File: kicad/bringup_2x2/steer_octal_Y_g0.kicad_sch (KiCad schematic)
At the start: 42 parts

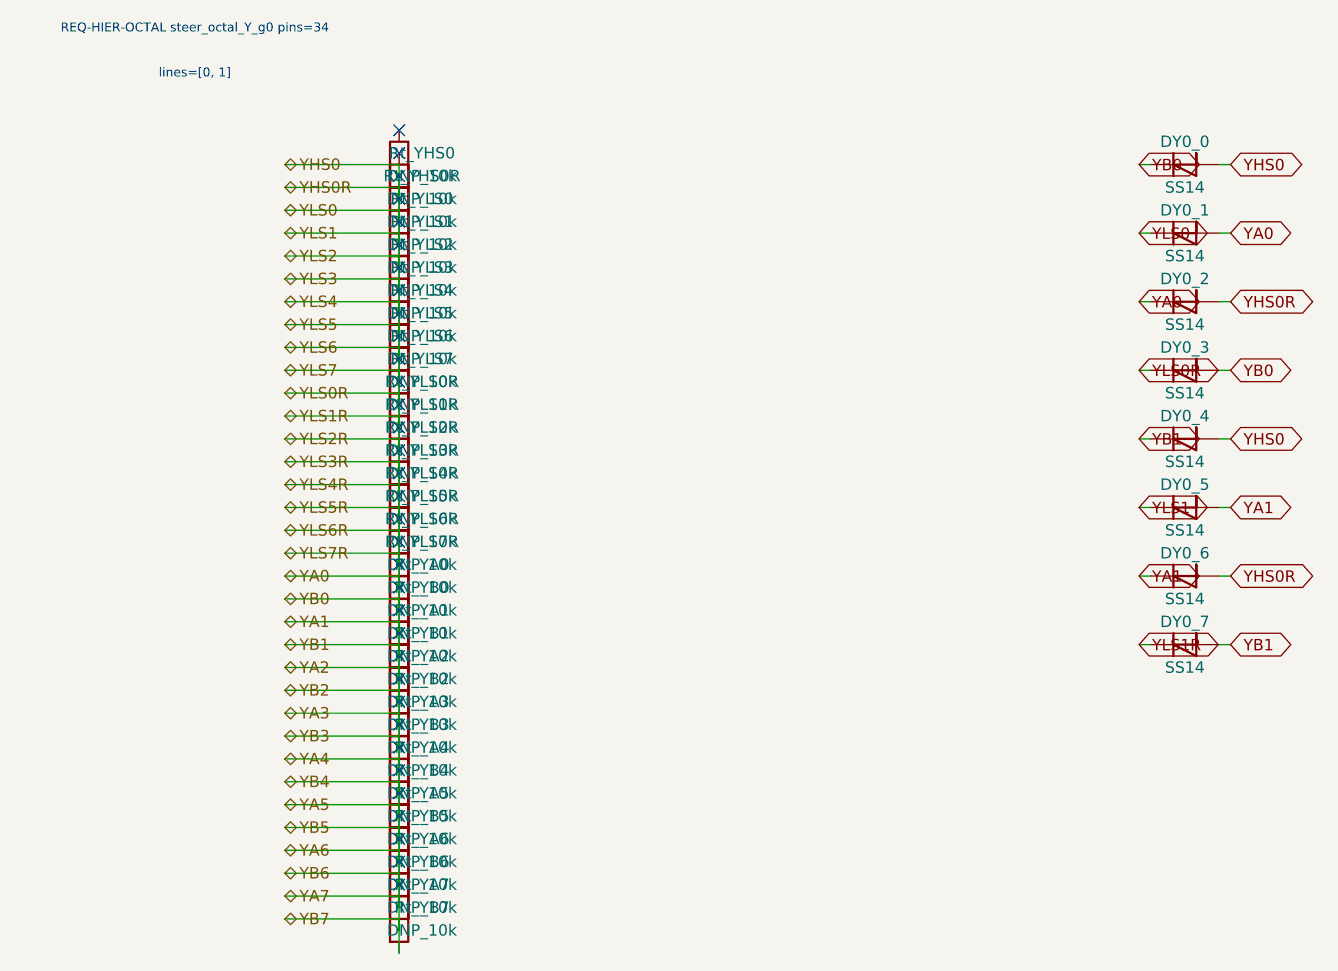
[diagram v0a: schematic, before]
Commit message: logical seperation into host and multiple decode/drive/steering boards
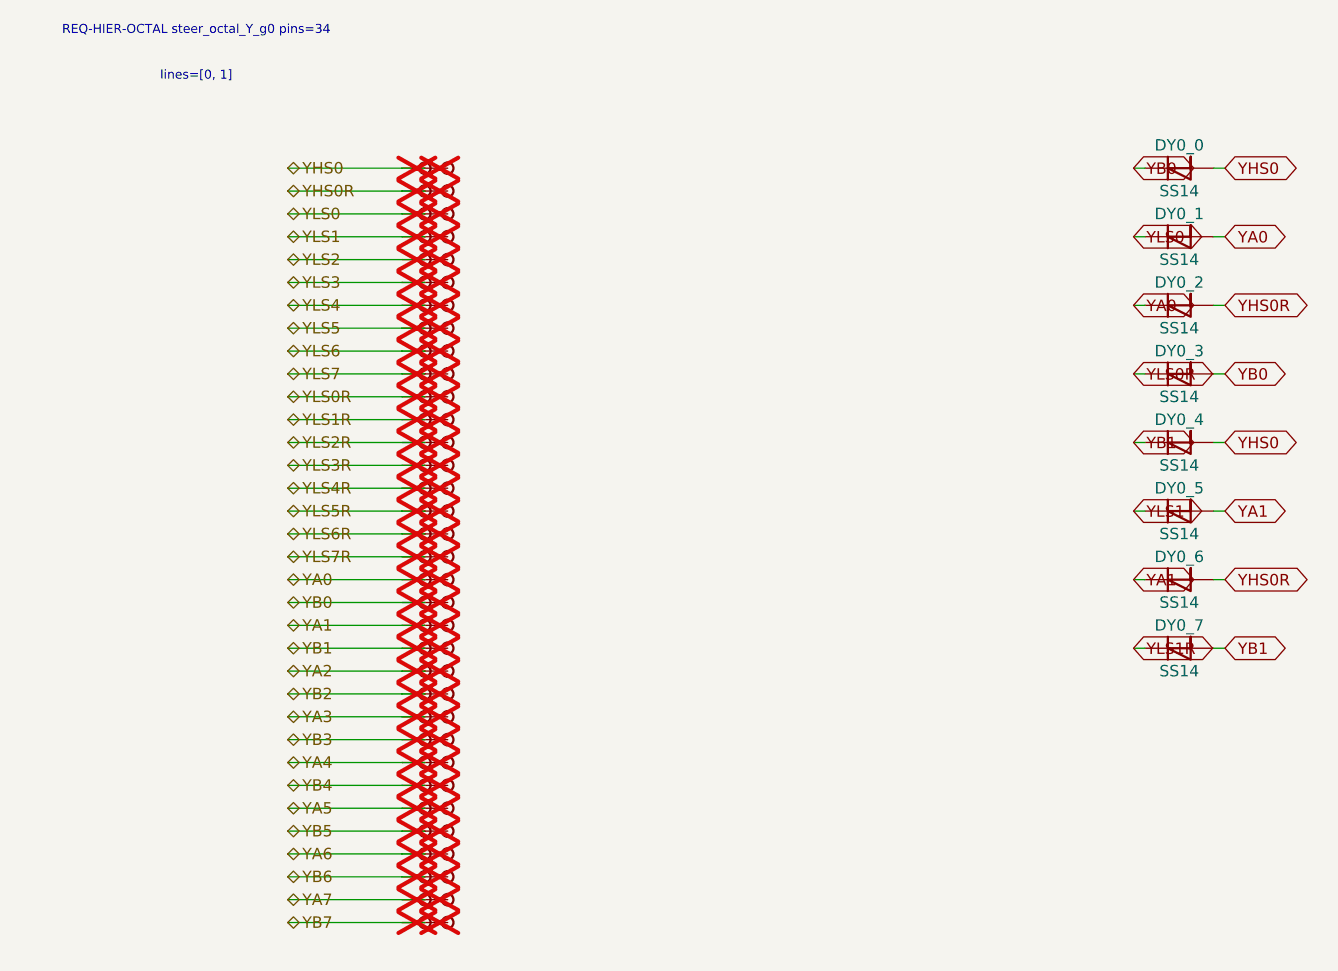
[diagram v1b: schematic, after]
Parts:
- removed Rt_YA0, Rt_YA1, Rt_YA2, Rt_YA3, Rt_YA4, Rt_YA5, Rt_YA6, Rt_YA7, Rt_YB0, Rt_YB1, Rt_YB2, Rt_YB3, Rt_YB4, Rt_YB5, Rt_YB6, Rt_YB7, Rt_YHS0, Rt_YHS0R, Rt_YLS0, Rt_YLS0R, Rt_YLS1, Rt_YLS1R, Rt_YLS2, Rt_YLS2R, Rt_YLS3, Rt_YLS3R, Rt_YLS4, Rt_YLS4R, Rt_YLS5, Rt_YLS5R, Rt_YLS6, Rt_YLS6R, Rt_YLS7, Rt_YLS7R: DNP_10k, symbol Device:R
- added TP_YA0, TP_YA0b, TP_YA1, TP_YA1b, TP_YA2, TP_YA2b, TP_YA3, TP_YA3b, TP_YA4, TP_YA4b, TP_YA5, TP_YA5b, TP_YA6, TP_YA6b, TP_YA7, TP_YA7b, TP_YB0, TP_YB0b, TP_YB1, TP_YB1b, TP_YB2, TP_YB2b, TP_YB3, TP_YB3b, TP_YB4, TP_YB4b, TP_YB5, TP_YB5b, TP_YB6, TP_YB6b, TP_YB7, TP_YB7b, TP_YHS0, TP_YHS0R, TP_YHS0Rb, TP_YHS0b, TP_YLS0, TP_YLS0R, TP_YLS0Rb, TP_YLS0b, TP_YLS1, TP_YLS1R, TP_YLS1Rb, TP_YLS1b, TP_YLS2, TP_YLS2R, TP_YLS2Rb, TP_YLS2b, TP_YLS3, TP_YLS3R, TP_YLS3Rb, TP_YLS3b, TP_YLS4, TP_YLS4R, TP_YLS4Rb, TP_YLS4b, TP_YLS5, TP_YLS5R, TP_YLS5Rb, TP_YLS5b, TP_YLS6, TP_YLS6R, TP_YLS6Rb, TP_YLS6b, TP_YLS7, TP_YLS7R, TP_YLS7Rb, TP_YLS7b: Stub, symbol CMR:Stub
- DY0_0, DY0_1, DY0_2, DY0_3, DY0_4, DY0_5, DY0_6, DY0_7: symbol Device:D_Schottky -> CMR:D_Schottky
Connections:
- net YA0: now also TP_YA0.1, TP_YA0b.1; no longer DY0_0.1 (K), DY0_0.2 (A), DY0_1.1 (K), DY0_2.2 (A), DY0_3.1 (K), DY0_3.2 (A), DY0_4.1 (K), DY0_4.2 (A), DY0_5.1 (K), DY0_5.2 (A), DY0_6.1 (K), DY0_6.2 (A), DY0_7.1 (K), DY0_7.2 (A)
- new net YA1: DY0_5.2 (A), DY0_6.1 (K), TP_YA1.1, TP_YA1b.1
- new net YA2: TP_YA2.1, TP_YA2b.1
- new net YA3: TP_YA3.1, TP_YA3b.1
- new net YA4: TP_YA4.1, TP_YA4b.1
- new net YA5: TP_YA5.1, TP_YA5b.1
- new net YA6: TP_YA6.1, TP_YA6b.1
- new net YA7: TP_YA7.1, TP_YA7b.1
- new net YB0: DY0_0.1 (K), DY0_3.2 (A), TP_YB0.1, TP_YB0b.1
- new net YB1: DY0_4.1 (K), DY0_7.2 (A), TP_YB1.1, TP_YB1b.1
- new net YB2: TP_YB2.1, TP_YB2b.1
- new net YB3: TP_YB3.1, TP_YB3b.1
- new net YB4: TP_YB4.1, TP_YB4b.1
- new net YB5: TP_YB5.1, TP_YB5b.1
- new net YB6: TP_YB6.1, TP_YB6b.1
- new net YB7: TP_YB7.1, TP_YB7b.1
- new net YHS0: DY0_0.2 (A), DY0_4.2 (A), TP_YHS0.1, TP_YHS0b.1
- new net YHS0R: DY0_2.2 (A), DY0_6.2 (A), TP_YHS0R.1, TP_YHS0Rb.1
- new net YLS0: DY0_1.1 (K), TP_YLS0.1, TP_YLS0b.1
- new net YLS0R: DY0_3.1 (K), TP_YLS0R.1, TP_YLS0Rb.1
- new net YLS1: DY0_5.1 (K), TP_YLS1.1, TP_YLS1b.1
- new net YLS1R: DY0_7.1 (K), TP_YLS1R.1, TP_YLS1Rb.1
- new net YLS2: TP_YLS2.1, TP_YLS2b.1
- new net YLS2R: TP_YLS2R.1, TP_YLS2Rb.1
- new net YLS3: TP_YLS3.1, TP_YLS3b.1
- new net YLS3R: TP_YLS3R.1, TP_YLS3Rb.1
- new net YLS4: TP_YLS4.1, TP_YLS4b.1
- new net YLS4R: TP_YLS4R.1, TP_YLS4Rb.1
- new net YLS5: TP_YLS5.1, TP_YLS5b.1
- new net YLS5R: TP_YLS5R.1, TP_YLS5Rb.1
- new net YLS6: TP_YLS6.1, TP_YLS6b.1
- new net YLS6R: TP_YLS6R.1, TP_YLS6Rb.1
- new net YLS7: TP_YLS7.1, TP_YLS7b.1
- new net YLS7R: TP_YLS7R.1, TP_YLS7Rb.1
- no-connect marks 34 -> 0
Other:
- moved on the sheet: DY0_0, DY0_1, DY0_2, DY0_3, DY0_4, DY0_5, DY0_6, DY0_7
